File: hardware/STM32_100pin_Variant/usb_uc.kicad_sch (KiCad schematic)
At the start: 23 parts, among them J3 , U1 STM32L4S7VITx, U2 ATA6561-GAQW-N, Y1 Crystal_GND24

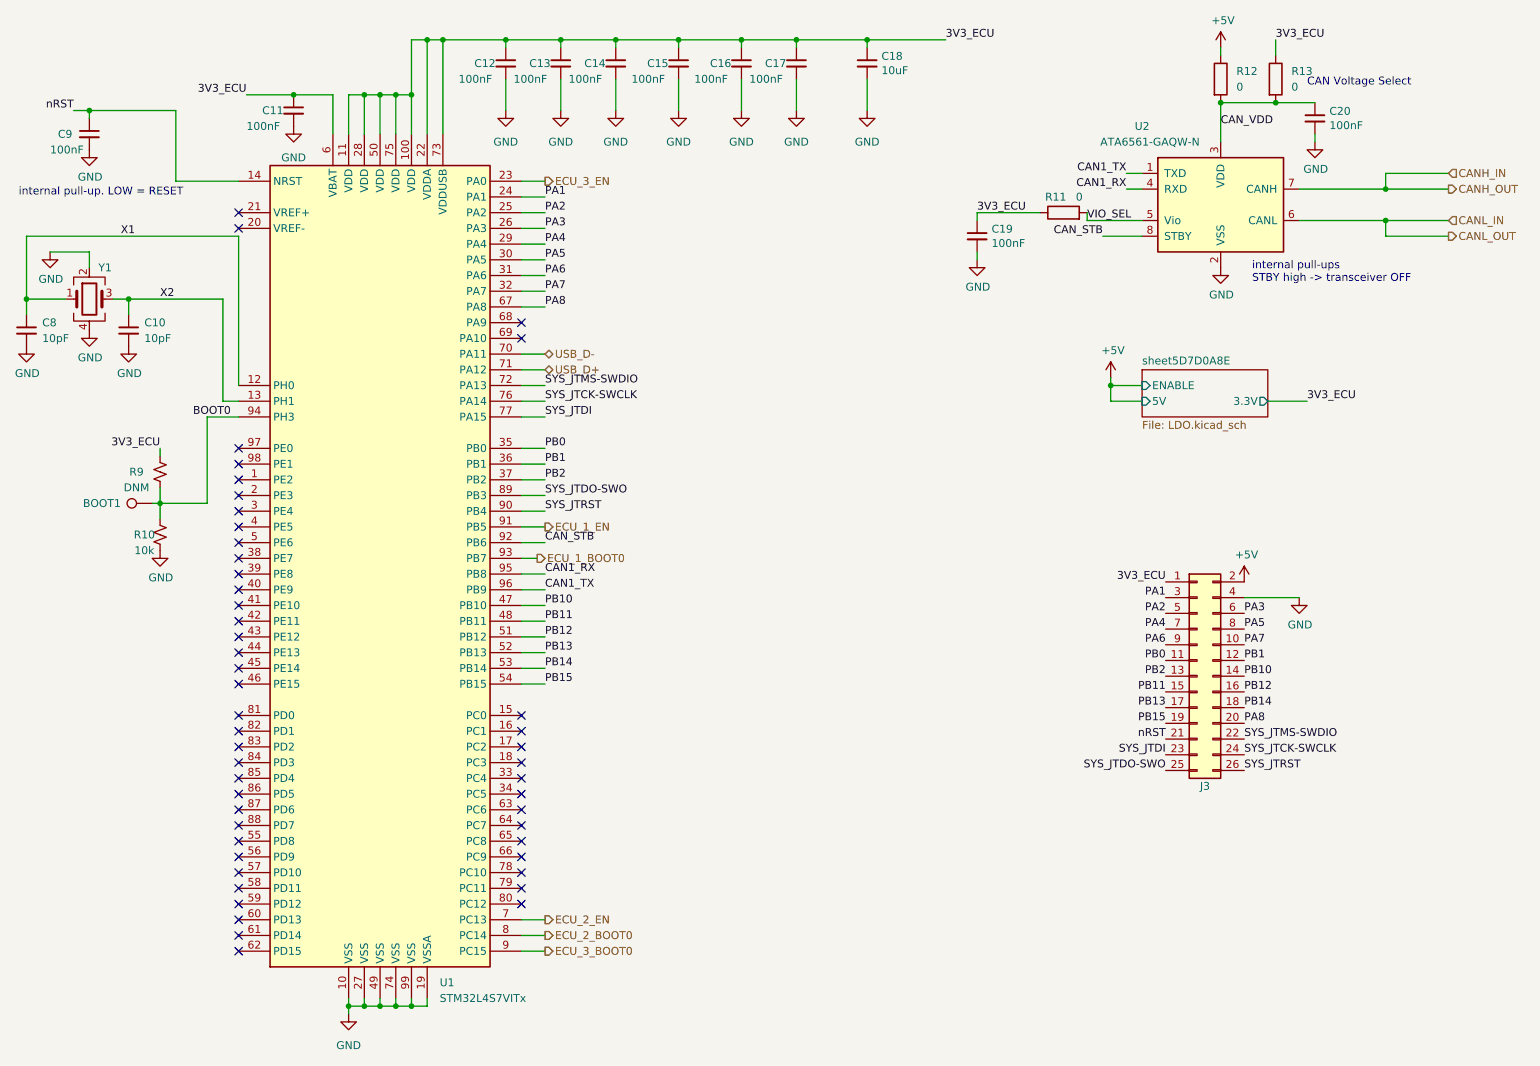
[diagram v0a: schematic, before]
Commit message: Schematic wiring fix, added part numbers
- Fixed missing connections between VREF+ and VDDA, VREF- and VSSA on all ECUs

- Added component part numbers for crystal and CAN trx to schematic
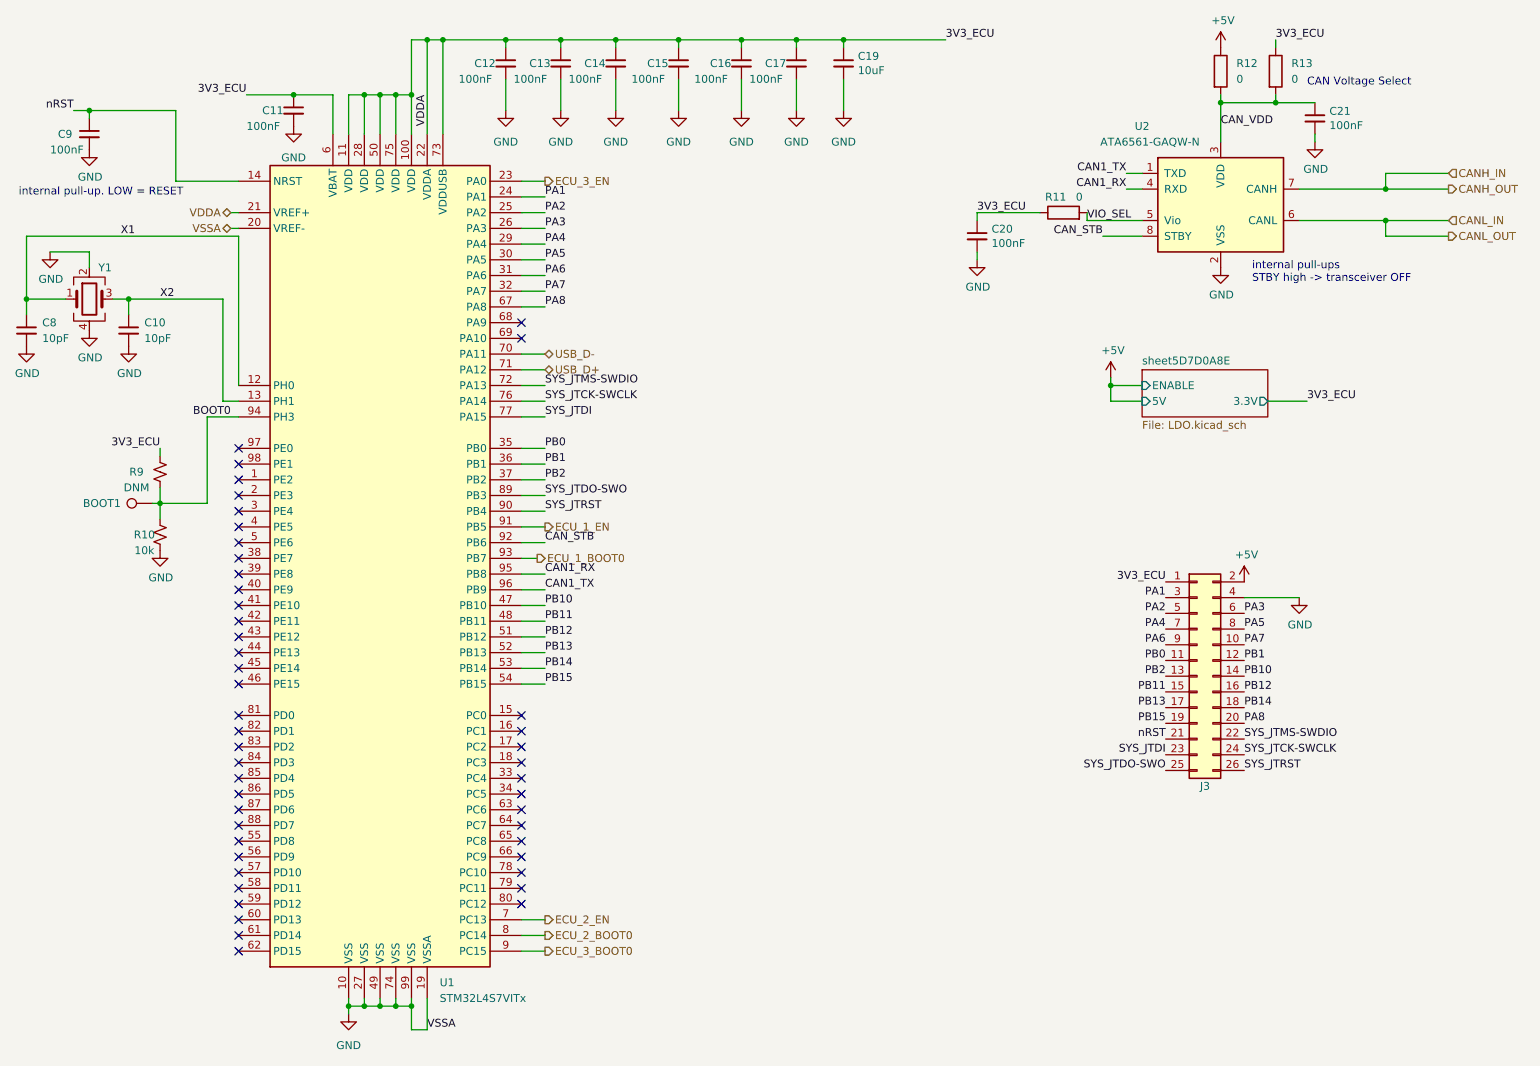
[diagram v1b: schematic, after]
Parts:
- U2: Part No. (none) -> TCAN1042HGVDRQ1
- Y1: Part No. (none) -> CX3225GB10000D0HEQCC
- renumbered C18 to C19, C19 to C20, C20 to C21
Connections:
- net 3V3_ECU is gone; now on net VDDA: C11.1, C12.1, C13.1, C14.1, C15.1, C16.1, C17.1, C19.1, C20.1, J3.1 (Pin_1), R11.1, R13.1, R9.1, U1.100 (VDD), U1.11 (VDD), U1.22 (VDDA), U1.28 (VDD), U1.50 (VDD), U1.6 (VBAT), U1.73 (VDDUSB), U1.75 (VDD)
- net GND: now also U1.20 (VREF-)
- net VDDA: now reaches U1.21 (VREF+)
- no-connect marks 49 -> 47
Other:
- moved on the sheet: C19, R12, R13

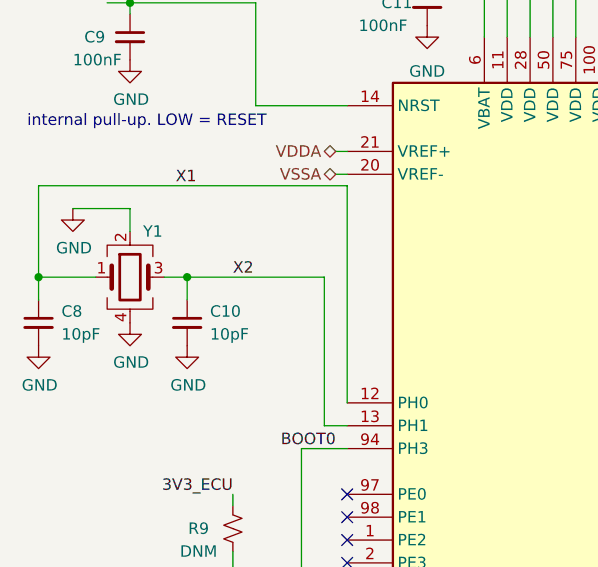
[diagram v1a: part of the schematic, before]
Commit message: Electrical Fix
- Fixed missing VREF+/- connections on ECUs

- Updated version number to V1.1

- Updated Gerbers

- Updated schematic PDF
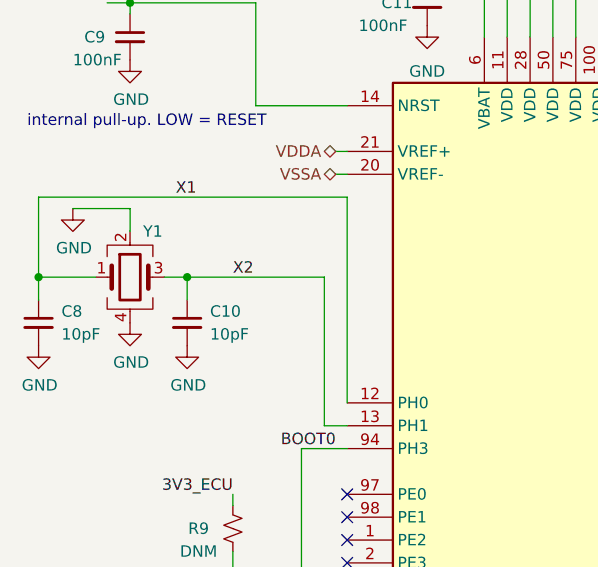
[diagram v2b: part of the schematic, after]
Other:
- title: RAMN: Resistant Automotive Miniature Network V1.0 -> RAMN 100 Pin Variant
